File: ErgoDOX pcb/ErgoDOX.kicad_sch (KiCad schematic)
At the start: 94 parts, among them J1 USB, J2 3.5mm, J3 JMP, J4 JMP, SW0:10 SW0:3, SW0:11 SW0:2, SW0:12 SW0:1, SW0:7 SW0:6, SW0:8 SW0:5, SW0:9 SW0:4, SW1:10 SW1:3, SW1:11 SW1:2, SW1:12 SW1:1, SW1:13 SW1:0, SW1:9 SW1:4, SW2:10 SW2:3, SW2:11 SW2:2, SW2:12 SW2:1, SW2:13 SW2:0, SW2:7 SW2:6, SW2:8 SW2:5, SW2:9 SW2:4, SW3:10 SW3:3, SW3:11 SW3:2, SW3:12 SW3:1, SW3:13 SW3:0, SW3:8 SW3:5, SW3:9 SW3:4, SW4:10 SW4:3, SW4:11 SW4:2, SW4:12 SW4:1, SW4:13 SW4:0, SW4:7 SW4:6, SW4:8 SW4:5, SW4:9 SW4:4, SW5:10 SW5:3, SW5:11 SW5:2, SW5:12 SW5:1, SW5:13 SW5:0, SW5:7 SW5:6, SW5:8 SW5:5, SW5:9 SW5:4, U1 TEENSY2.0, U2 MCP23018

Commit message: Fixed footprints and changed LEDs layout
Signed-off-by: Todor Todorov <todor@meltoactive.com>
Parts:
- removed D1, D10, D11, D12, D13, D14, D15, D16, D17, D18, D19, D2, D20, D21, D22, D23, D24, D25, D26, D27, D28, D29, D3, D30, D31, D32, D33, D34, D35, D36, D37, D38, D4, D5, D6, D7, D8, D9: SK6812MINI-E, tt-diodes:SK6812MINI-E_3.2x2.8_double_reversed, symbol tnt_diodes:SK6812MINI-E
- removed JP1, JP2: JUMPER, symbol ErgoDOX-rescue:JUMPER
- removed SW0:10: SW0:3, tt-switches:MX_FLIP_DIODE, symbol ErgoDOX-rescue:SWITCH_DIODE
- removed SW0:11: SW0:2, tt-switches:MX_FLIP_DIODE, symbol ErgoDOX-rescue:SWITCH_DIODE
- removed SW0:12: SW0:1, tt-switches:MX_FLIP_DIODE, symbol ErgoDOX-rescue:SWITCH_DIODE
- removed SW0:7: SW0:6, tt-switches:MX_FLIP_DIODE, symbol ErgoDOX-rescue:SWITCH_DIODE
- removed SW0:8: SW0:5, tt-switches:MX_FLIP_DIODE, symbol ErgoDOX-rescue:SWITCH_DIODE
- removed SW0:9: SW0:4, tt-switches:MX_FLIP_DIODE, symbol ErgoDOX-rescue:SWITCH_DIODE
- removed SW1:10: SW1:3, tt-switches:MX_FLIP_DIODE, symbol ErgoDOX-rescue:SWITCH_DIODE
- removed SW1:11: SW1:2, tt-switches:MX_FLIP_DIODE, symbol ErgoDOX-rescue:SWITCH_DIODE
- removed SW1:12: SW1:1, tt-switches:MX_FLIP_DIODE, symbol ErgoDOX-rescue:SWITCH_DIODE
- removed SW1:13: SW1:0, tt-switches:MX_FLIP_DIODE, symbol ErgoDOX-rescue:SWITCH_DIODE
- removed SW1:9: SW1:4, tt-switches:MX_FLIP_DIODE, symbol ErgoDOX-rescue:SWITCH_DIODE
- removed SW2:10: SW2:3, tt-switches:MX_FLIP_DIODE, symbol ErgoDOX-rescue:SWITCH_DIODE
- removed SW2:11: SW2:2, tt-switches:MX_FLIP_DIODE, symbol ErgoDOX-rescue:SWITCH_DIODE
- removed SW2:12: SW2:1, tt-switches:MX_FLIP_DIODE, symbol ErgoDOX-rescue:SWITCH_DIODE
- removed SW2:13: SW2:0, tt-switches:MX_FLIP_DIODE, symbol ErgoDOX-rescue:SWITCH_DIODE
- removed SW2:7: SW2:6, tt-switches:MX_FLIP_DIODE, symbol ErgoDOX-rescue:SWITCH_DIODE
- removed SW2:8: SW2:5, tt-switches:MX_FLIP_DIODE, symbol ErgoDOX-rescue:SWITCH_DIODE
- removed SW2:9: SW2:4, tt-switches:MX_FLIP_DIODE, symbol ErgoDOX-rescue:SWITCH_DIODE
- removed SW3:10: SW3:3, tt-switches:MX_FLIP_DIODE, symbol ErgoDOX-rescue:SWITCH_DIODE
- removed SW3:11: SW3:2, tt-switches:MX_FLIP_DIODE, symbol ErgoDOX-rescue:SWITCH_DIODE
- removed SW3:12: SW3:1, tt-switches:MX_FLIP_DIODE, symbol ErgoDOX-rescue:SWITCH_DIODE
- removed SW3:13: SW3:0, tt-switches:MX_FLIP_DIODE, symbol ErgoDOX-rescue:SWITCH_DIODE
- removed SW3:8: SW3:5, tt-switches:MX_FLIP_DIODE, symbol ErgoDOX-rescue:SWITCH_DIODE
- removed SW3:9: SW3:4, tt-switches:MX_FLIP_DIODE, symbol ErgoDOX-rescue:SWITCH_DIODE
- removed SW4:10: SW4:3, tt-switches:MX_FLIP_DIODE, symbol ErgoDOX-rescue:SWITCH_DIODE
- removed SW4:11: SW4:2, tt-switches:MX_FLIP_DIODE, symbol ErgoDOX-rescue:SWITCH_DIODE
- removed SW4:12: SW4:1, tt-switches:MX_FLIP_DIODE, symbol ErgoDOX-rescue:SWITCH_DIODE
- removed SW4:13: SW4:0, tt-switches:MX_FLIP_DIODE, symbol ErgoDOX-rescue:SWITCH_DIODE
- removed SW4:7: SW4:6, tt-switches:MX_FLIP_DIODE, symbol ErgoDOX-rescue:SWITCH_DIODE
- removed SW4:8: SW4:5, tt-switches:MX_FLIP_DIODE, symbol ErgoDOX-rescue:SWITCH_DIODE
- removed SW4:9: SW4:4, tt-switches:MX_FLIP_DIODE, symbol ErgoDOX-rescue:SWITCH_DIODE
- removed SW5:10: SW5:3, tt-switches:MX_FLIP_DIODE, symbol ErgoDOX-rescue:SWITCH_DIODE
- removed SW5:11: SW5:2, tt-switches:MX_FLIP_DIODE, symbol ErgoDOX-rescue:SWITCH_DIODE
- removed SW5:12: SW5:1, tt-switches:MX_FLIP_DIODE, symbol ErgoDOX-rescue:SWITCH_DIODE
- removed SW5:13: SW5:0, tt-switches:MX_FLIP_DIODE, symbol ErgoDOX-rescue:SWITCH_DIODE
- removed SW5:7: SW5:6, tt-switches:MX_FLIP_DIODE, symbol ErgoDOX-rescue:SWITCH_DIODE
- removed SW5:8: SW5:5, tt-switches:MX_FLIP_DIODE, symbol ErgoDOX-rescue:SWITCH_DIODE
- removed SW5:9: SW5:4, tt-switches:MX_FLIP_DIODE, symbol ErgoDOX-rescue:SWITCH_DIODE
- J3, J4: footprint (none) -> Connector_PinHeader_2.54mm:PinHeader_1x03_P2.54mm_Vertical
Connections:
- net COL1: no longer U1.10 (PD3)
- net COL10: no longer U2.23 (GPA3)
- net COL11: no longer U2.22 (GPA2)
- net COL4: no longer U1.4 (PB2)
- net COL5: no longer U1.3 (PB1)
- net COL6: no longer U1.2 (PB0)
- net RGB: now also R5.1, R6.1, U1.6 (PB7), U2.27 (GPA7); no longer R5.2, R6.2
- net at U2.10 (GPB7): no longer R6.1
- net LED_ON: now reaches U2.9 (GPB6)
- net LED_ON: now also U1.11 (PC6)
- new net COL12: U1.10 (PD3)
- new net COL2: U2.22 (GPA2)
- new net COL3: U2.23 (GPA3)
- new net COL7: U1.2 (PB0)
- new net COL8: U1.3 (PB1)
- new net COL9: U1.4 (PB2)
- new net LEDs/RGB: R5.2, R6.2
- no-connect marks 20 -> 15
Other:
- added sheet Keys (ErgoDOX_keys.kicad_sch)
- added sheet LEDs (ErgoDOX_leds.kicad_sch)
- moved on the sheet: H99, J1, J2, J3, J4, R1, R2, R3, R4, R5, R6, S1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

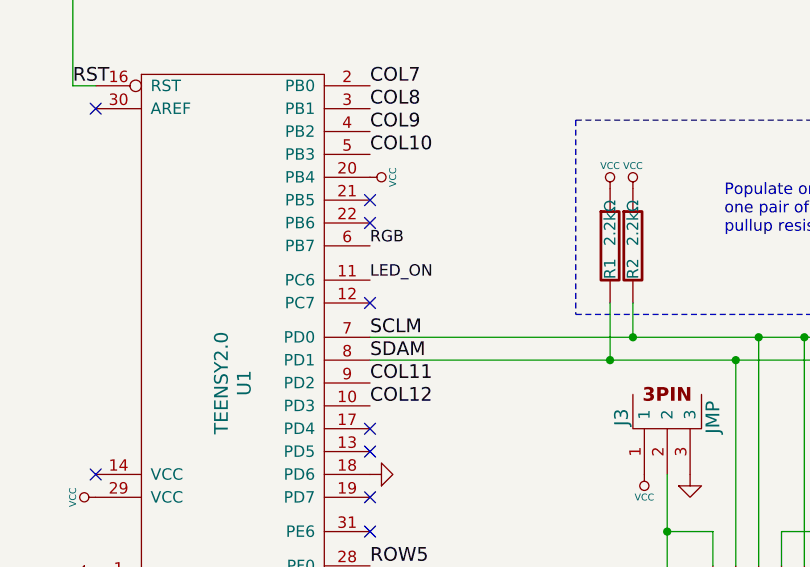
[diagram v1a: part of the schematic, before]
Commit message: Fix connection to COL13
Signed-off-by: Todor Todorov <todor@meltoactive.com>
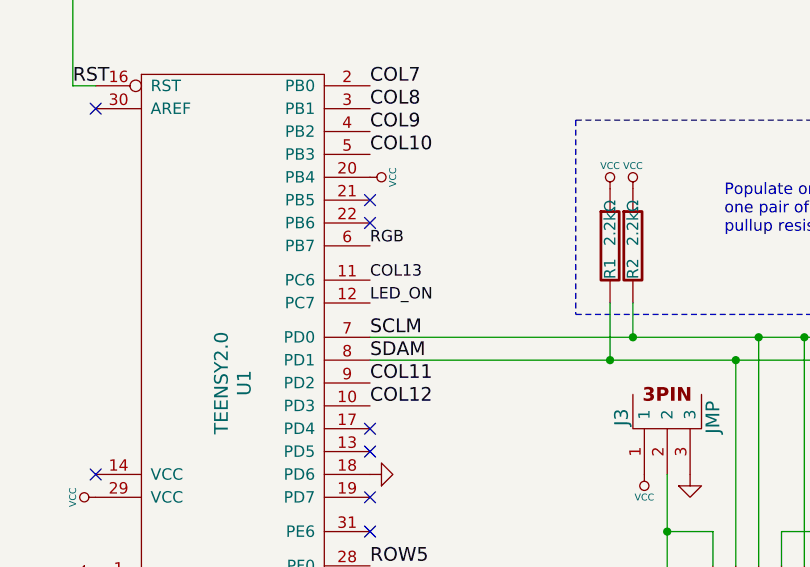
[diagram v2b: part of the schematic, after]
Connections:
- net COL13: now also U1.11 (PC6)
- net LED_ON: now also U1.12 (PC7); no longer U1.11 (PC6)
- no-connect marks 15 -> 14
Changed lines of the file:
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@@
   (no_connect (at 82.55 48.26))
   (no_connect (at 82.55 50.8))
-  (no_connect (at 82.55 59.69))
   (no_connect (at 82.55 73.66))
   (no_connect (at 82.55 76.2))
@@
     (effects (font (size 1.27 1.27)) (justify left bottom))
   )
-  (label "LED_ON" (at 82.55 57.15 0)
-    (effects (font (size 1.27 1.27)) (justify left bottom))
-  )
+  (label "COL13" (at 82.55 57.15 0)
+    (effects (font (size 1.27 1.27)) (justify left bottom))
+  )
+  (label "LED_ON" (at 82.55 59.69 0)
+    (effects (font (size 1.27 1.27)) (justify left bottom))
+  )
